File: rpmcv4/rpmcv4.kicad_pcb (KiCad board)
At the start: 2 copper layers, 88.3 x 97.8 mm, 31 parts, among them J1 RPi_GPIO, P1 CONN_02X25, P2 CONN_02X25, U1 74LS373, U2 74LS373, U3 74LS245, U7 74LS245, U8 74LS245

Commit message: small improvement
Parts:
- added REF3: MountingHole_2.7mm_Pad, Mounting_Holes:MountingHole_2.7mm_Pad, F.Cu at (132.6, 122.2)
- added REF4: MountingHole_2.7mm_Pad, Mounting_Holes:MountingHole_2.7mm_Pad, F.Cu at (210.3, 122.2)
- U1, U2, U3, U7, U8: footprint Housings_DIP:DIP-20_W7.62mm -> Housings_SOIC:SOIC-20_7.5x12.8mm_Pitch1.27mm; moved to B.Cu
- moved U8 19.7 mm to (141.0, 74.9), turned to 270 degrees
- moved P1 18.1 mm to (172.5, 113.1)
- moved P2 18.1 mm to (172.5, 92.5)
- moved R11 18.1 mm to (148.4, 99.8)
- moved R10 18.1 mm to (148.5, 120.4)
- moved D1 16.6 mm to (206.8, 127.0)
- moved D2 16.6 mm to (201.7, 127.0)
- moved D3 16.6 mm to (194.1, 127.0)
- moved D4 16.6 mm to (189.0, 127.0)
- moved D5 16.6 mm to (183.9, 127.0)
- moved D6 16.6 mm to (178.8, 127.0)
- moved R1 16.6 mm to (205.5, 128.2)
- moved R2 16.6 mm to (200.4, 128.3)
- moved R3 16.6 mm to (192.8, 128.3)
- moved R4 16.6 mm to (187.7, 128.3)
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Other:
- board size 88.3 x 97.8 mm -> 85.1 x 81.3 mm

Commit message: update for rpmcv1 and rpspc
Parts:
- removed U7, U8: 74LS245, Housings_SOIC:SOIC-20_7.5x12.8mm_Pitch1.27mm
- added G1: LOGO, MSX:msx_msx2_msx+logo, F.Cu at (171.4, 73.5)
- added U4: 74LS245, Housings_SOIC:SOIC-20W_7.5x12.8mm_Pitch1.27mm, B.Cu at (188.0, 76.2)
- added U5: 74LS245, Housings_SOIC:SOIC-20W_7.5x12.8mm_Pitch1.27mm, B.Cu at (138.4, 76.2)
- U1, U2, U3: footprint Housings_SOIC:SOIC-20_7.5x12.8mm_Pitch1.27mm -> Housings_SOIC:SOIC-20W_7.5x12.8mm_Pitch1.27mm
- moved U3 17.8 mm to (204.5, 76.2)
- moved U2 1.80 mm to (154.9, 76.2)
- moved U1 1.27 mm to (171.4, 76.2)
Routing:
- net +3V3: track 0.00 -> 198.8 mm
- net /WR: track 0.00 -> 146.8 mm, vias 0 -> 1
- net /HAN: track 0.00 -> 139.7 mm
- net +5V: track 0.00 -> 139.6 mm, vias 0 -> 4
- net GND: track 0.00 -> 121.4 mm, vias 0 -> 13
- net /PWR: track 0.00 -> 107.6 mm
- net /RD7: track 0.00 -> 101.4 mm
- net /LE_B: track 0.00 -> 86.2 mm, vias 0 -> 3
- net /CLK: track 0.00 -> 86.2 mm, vias 0 -> 1
- net /CAPS: track 0.00 -> 82.4 mm
- net /RD2: track 0.00 -> 78.0 mm
- net /SW1: track 0.00 -> 73.5 mm
- net /RA11: track 0.00 -> 71.4 mm, vias 0 -> 1
- net /RD4: track 0.00 -> 69.7 mm, vias 0 -> 2
- net /SLTSL1: track 0.00 -> 62.9 mm
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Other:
- board text added: "74HC245"
- board text added: "74HC373"
- board text added: "rp"

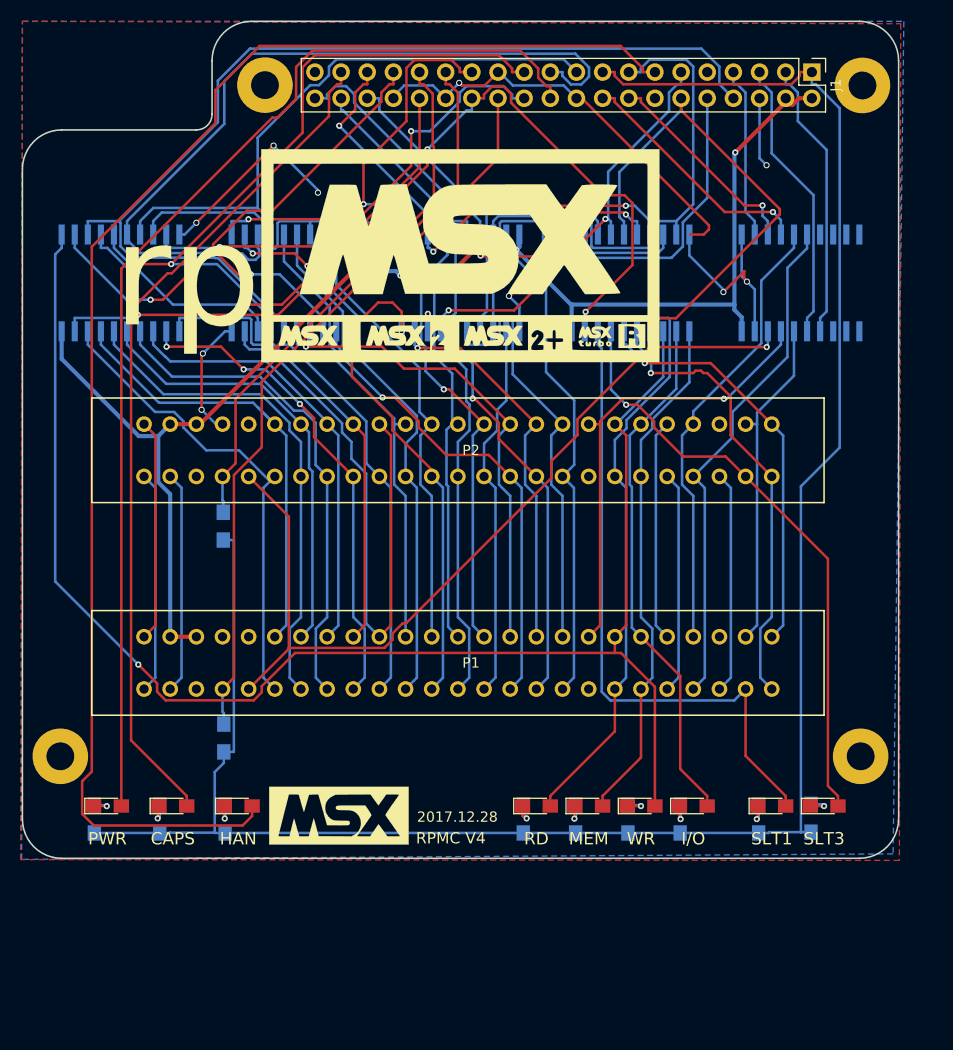
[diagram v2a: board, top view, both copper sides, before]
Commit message: modification for rpmcv4 and rpibox
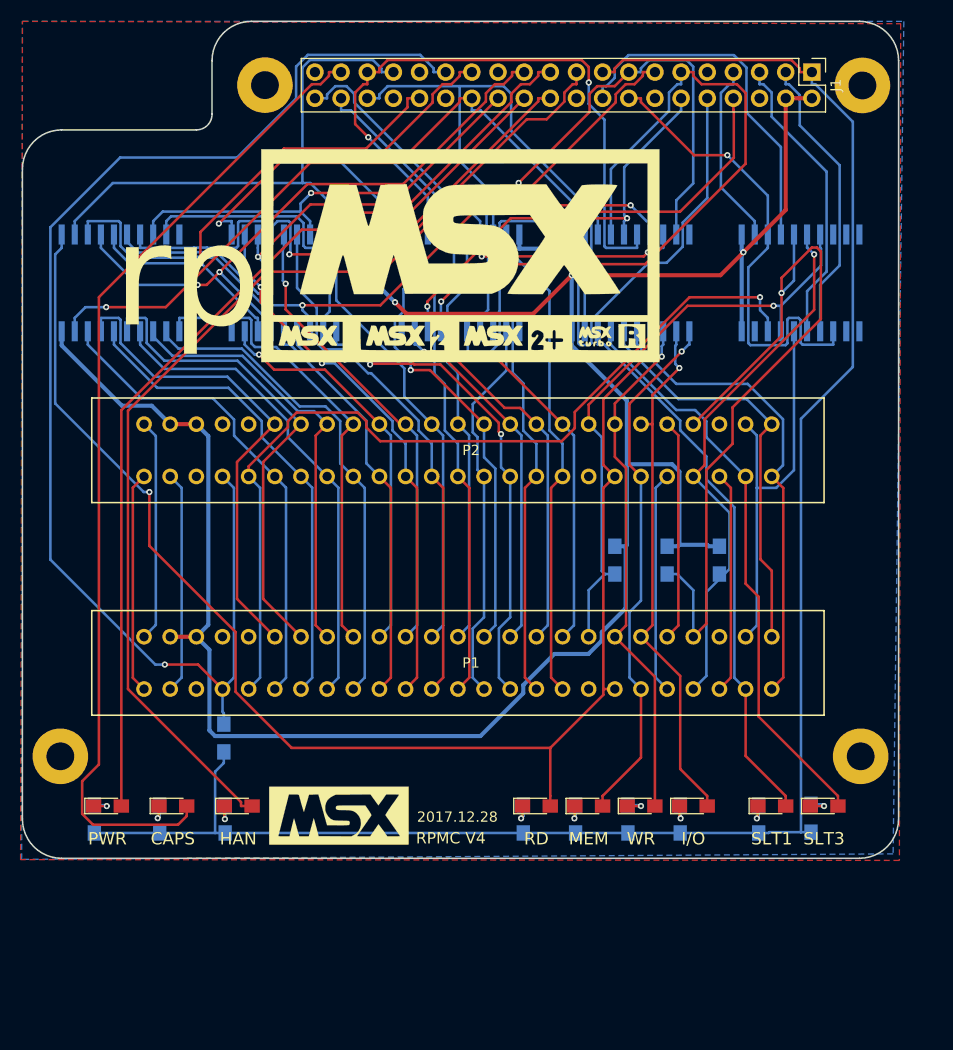
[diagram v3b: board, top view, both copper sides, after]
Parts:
- added R12: R, Resistors_SMD:R_0805_HandSoldering, B.Cu at (191.5, 103.1)
- added R13: R, Resistors_SMD:R_0805_HandSoldering, B.Cu at (186.4, 103.1)
- moved R11 48.3 mm to (196.6, 103.1)
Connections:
- J1 pad 31: /SW3 -> Net-(J1-Pad31)
- P2 pad 44: /SW3 -> /SW1
- R11 pad 1: +3V3 -> /INT
- R11 pad 2: /SW3 -> +5V
- U3 pad 1: GND -> +5V
- U3 pad 13: Net-(U3-Pad13) -> /RRESET
- U3 pad 7: Net-(U3-Pad7) -> /RESET
- U4 pad 1: GND -> +5V
- U5 pad 1: /WR -> /RD
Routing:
- net GND: track 121.4 -> 0.00 mm, vias 13 -> 0
- net +5V: track 139.6 -> 236.1 mm, vias 4 -> 3
- net /WR: track 146.8 -> 50.6 mm
- net /RD: track 56.2 -> 137.7 mm, vias 0 -> 2
- net /SW1: track 73.5 -> 127.3 mm, vias 0 -> 1
- net /SW3: track 52.1 -> 0.00 mm
- net /WAIT: track 44.0 -> 79.4 mm, vias 0 -> 1
- net /RA10: track 40.6 -> 71.0 mm, vias 2 -> 1
- net /HAN: track 139.7 -> 109.5 mm
- net /RA11: track 71.4 -> 41.4 mm, vias 1 -> 2
- net /RRESET: track 20.6 -> 47.2 mm
- net +3V3: track 198.8 -> 177.3 mm
- net /RD2: track 78.0 -> 58.9 mm, vias 0 -> 1
- net /RA12: track 45.7 -> 64.5 mm, vias 3 -> 2
- net /A5: track 57.7 -> 39.1 mm, vias 0 -> 1
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
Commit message: minor update for rpspc, rpmcv4, rpmpv1
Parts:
- removed G1: LOGO, MSX:msx_msx2_msx+logo
- added G***: LOGO, 8BIT:raspberry_pi_logo, F.Cu at (158.4, 72.3)
- added G***: LOGO, 8BIT:msx_msx2_msx+logo, F.Cu at (177.7, 72.0)
- added R14: R, Resistors_SMD:R_0805_HandSoldering, B.Cu at (187.7, 119.9)
- added R15: R, Resistors_SMD:R_0805_HandSoldering, B.Cu at (193.0, 119.9)
- added R16: R, Resistors_SMD:R_0805_HandSoldering, B.Cu at (190.5, 119.9)
- added R17: R, Resistors_SMD:R_0805_HandSoldering, B.Cu at (184.9, 119.9)
- added R18: R, Resistors_SMD:R_0805_HandSoldering, B.Cu at (201.9, 119.9)
- added R19: R, Resistors_SMD:R_0805_HandSoldering, B.Cu at (199.1, 119.9)
- J1: footprint Pin_Headers:Pin_Header_Straight_2x20_Pitch2.54mm -> Socket_Strips:Socket_Strip_Straight_2x20_Pitch2.54mm; moved to B.Cu
- turned J1 to 90 degrees
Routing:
- net GND: track 0.00 -> 72.5 mm, vias 0 -> 16
- net +5V: track 236.1 -> 268.7 mm
- net /RD: track 137.7 -> 141.2 mm
- net /MREQ: track 51.5 -> 54.9 mm
- net /RCS12: track 35.0 -> 36.4 mm
- net /RRESET: track 47.2 -> 48.3 mm
- net /SLTSL3: track 56.3 -> 57.4 mm, vias 0 -> 1
- net /WR: track 50.6 -> 51.3 mm, vias 1 -> 2
- net /IORQ: track 51.6 -> 52.0 mm, vias 1 -> 2
- net /SLTSL1: track 54.0 -> 54.1 mm, vias 0 -> 1
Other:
- board text added: "2018.1.19"
- board text added: "Raspberry Pi MSX Clone"
- board text added: "SLT2"
- board text added: "meeso.kim@gmail.com"
- board text removed: "2017.12.28"
- board text removed: "SLT3"
- board text removed: "rp"

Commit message: clean up for all works
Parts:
- turned D1 to 180 degrees
- turned D2 to 180 degrees
- turned D3 to 180 degrees
- turned D4 to 180 degrees
- turned D5 to 180 degrees
- turned D6 to 180 degrees
- turned D7 to 180 degrees
- turned D8 to 180 degrees
- turned D9 to 180 degrees
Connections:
- D1 pad 1: Net-(D1-Pad1) -> /SLTSL3
- D1 pad 2: /SLTSL3 -> Net-(D1-Pad2)
- D2 pad 1: Net-(D2-Pad1) -> /SLTSL1
- D2 pad 2: /SLTSL1 -> Net-(D2-Pad2)
- D3 pad 1: Net-(D3-Pad1) -> /IORQ
- D3 pad 2: /IORQ -> Net-(D3-Pad2)
- D4 pad 1: Net-(D4-Pad1) -> /WR
- D4 pad 2: /WR -> Net-(D4-Pad2)
- D5 pad 1: Net-(D5-Pad1) -> /MREQ
- D5 pad 2: /MREQ -> Net-(D5-Pad2)
- D6 pad 1: Net-(D6-Pad1) -> /RD
- D6 pad 2: /RD -> Net-(D6-Pad2)
- D7 pad 1: Net-(D7-Pad1) -> /HAN
- D7 pad 2: /HAN -> Net-(D7-Pad2)
- D8 pad 1: Net-(D8-Pad1) -> /CAPS
- D8 pad 2: /CAPS -> Net-(D8-Pad2)
- D9 pad 1: Net-(D9-Pad1) -> /PWR
- D9 pad 2: /PWR -> Net-(D9-Pad2)
- R1 pad 2: Net-(D1-Pad1) -> Net-(D1-Pad2)
- R2 pad 2: Net-(D2-Pad1) -> Net-(D2-Pad2)
- R3 pad 2: Net-(D3-Pad1) -> Net-(D3-Pad2)
- R4 pad 2: Net-(D4-Pad1) -> Net-(D4-Pad2)
- R5 pad 2: Net-(D5-Pad1) -> Net-(D5-Pad2)
- R6 pad 2: Net-(D6-Pad1) -> Net-(D6-Pad2)
- R7 pad 2: Net-(D7-Pad1) -> Net-(D7-Pad2)
- R8 pad 2: Net-(D8-Pad1) -> Net-(D8-Pad2)
- R9 pad 2: Net-(D9-Pad1) -> Net-(D9-Pad2)
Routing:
- net Net-(D1-Pad2): track 0.00 -> 2.69 mm, vias 0 -> 1
- net Net-(D1-Pad1): track 2.69 -> 0.00 mm, vias 1 -> 0
- net Net-(D4-Pad2): track 0.00 -> 2.66 mm, vias 0 -> 1
- net Net-(D4-Pad1): track 2.66 -> 0.00 mm, vias 1 -> 0
- net Net-(D7-Pad2): track 0.00 -> 2.65 mm, vias 0 -> 1
- net Net-(D7-Pad1): track 2.65 -> 0.00 mm, vias 1 -> 0
- net Net-(D6-Pad2): track 0.00 -> 2.63 mm, vias 0 -> 1
- net Net-(D6-Pad1): track 2.63 -> 0.00 mm, vias 1 -> 0
- net Net-(D2-Pad2): track 0.00 -> 2.60 mm, vias 0 -> 1
- net Net-(D2-Pad1): track 2.60 -> 0.00 mm, vias 1 -> 0
- net Net-(D8-Pad2): track 0.00 -> 2.58 mm, vias 0 -> 1
- net Net-(D8-Pad1): track 2.58 -> 0.00 mm, vias 1 -> 0
- net Net-(D3-Pad2): track 0.00 -> 2.55 mm, vias 0 -> 1
- net Net-(D3-Pad1): track 2.55 -> 0.00 mm, vias 1 -> 0
- net Net-(D5-Pad2): track 0.00 -> 2.55 mm, vias 0 -> 1
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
